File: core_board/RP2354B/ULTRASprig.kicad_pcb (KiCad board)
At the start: 2 copper layers, 34.1 x 53.9 mm, 47 parts, among them J1 Conn_01x06_Pin, J10 Conn_01x10_Pin, J2 USB_C_Receptacle_USB2.0_14P, J3 Conn_01x02_Pin, J4 Conn_01x12_Pin, J6 Conn_01x10_Pin, U1 RP2354B, U2 USBLC6-2P6, U3 BQ24230RGT, U4 TPS62130A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

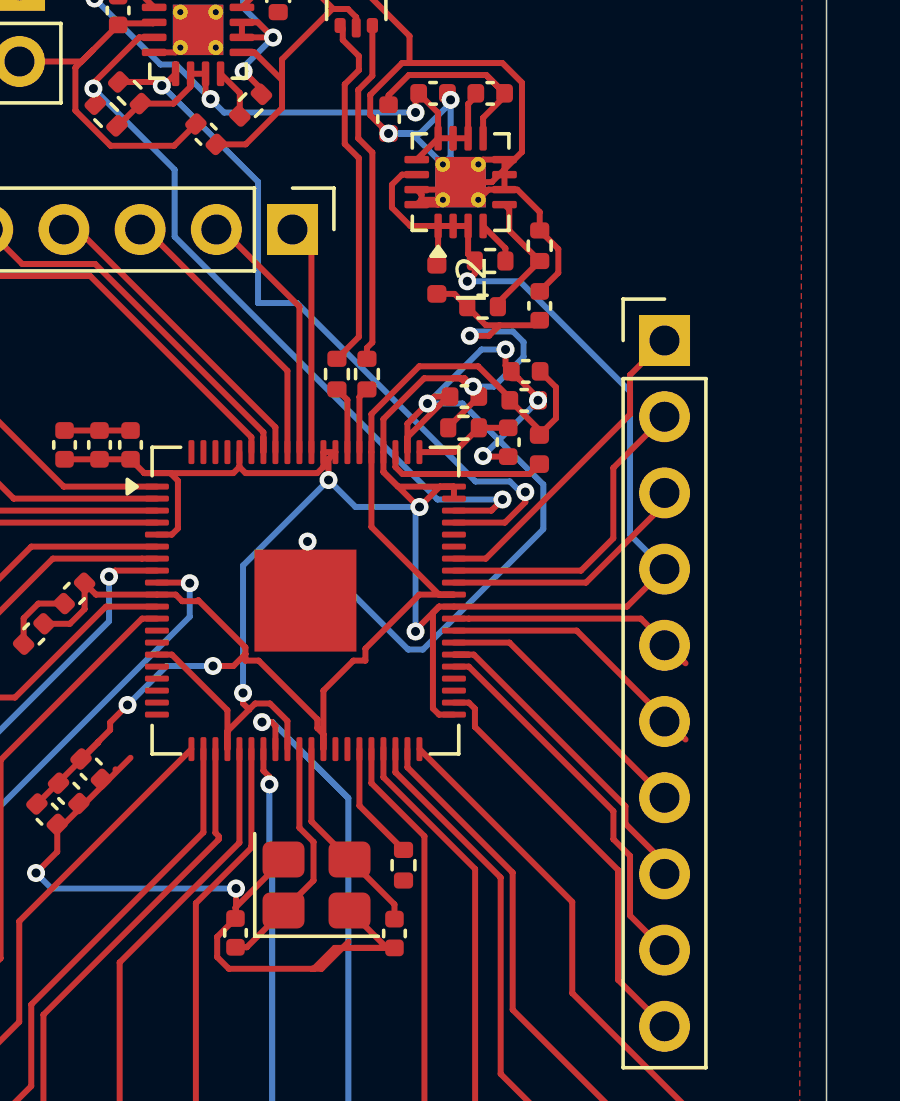
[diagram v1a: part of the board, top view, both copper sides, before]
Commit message: add RP2354 BoM
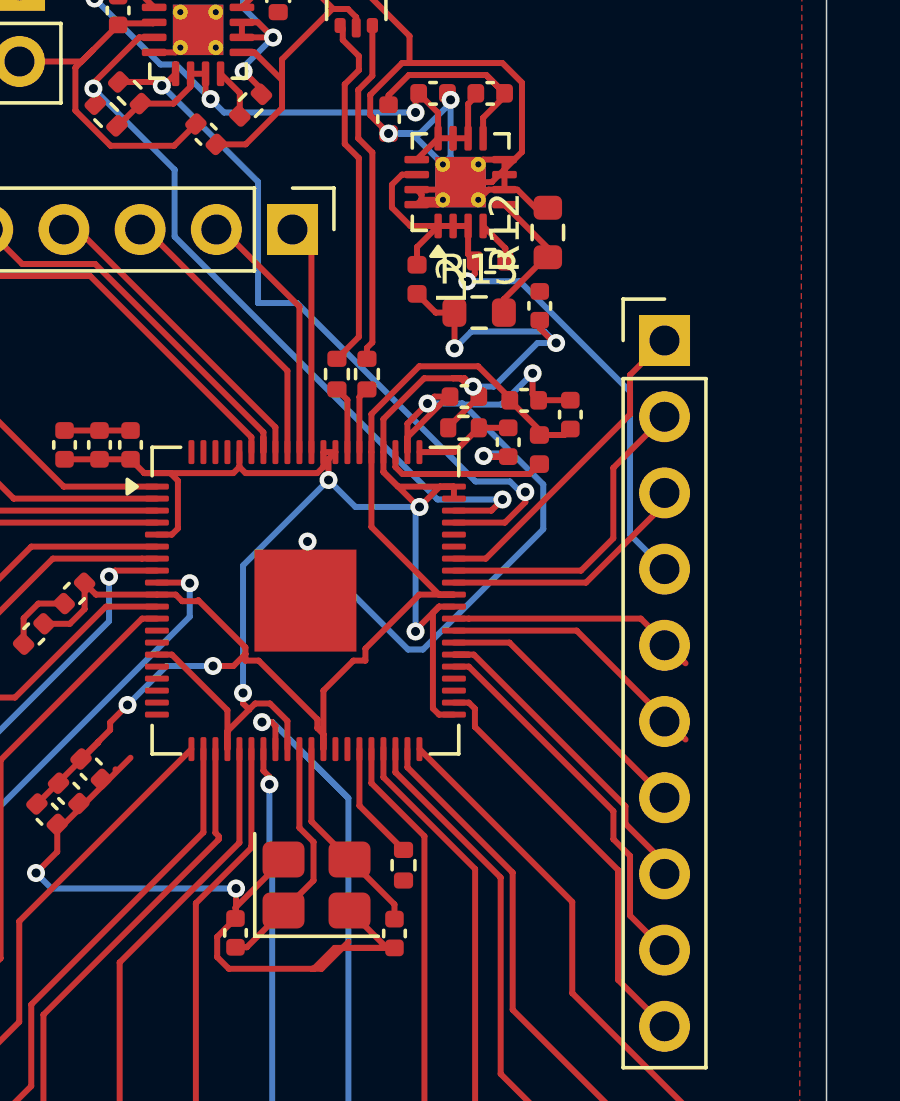
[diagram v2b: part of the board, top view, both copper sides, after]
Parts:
- R12: value 9K -> 8K; footprint Resistor_SMD:R_0402_1005Metric -> Resistor_SMD:R_0603_1608Metric
- R13: value 2K -> 25K; footprint Resistor_SMD:R_0402_1005Metric -> Resistor_SMD:R_0603_1608Metric
- moved C10 2.07 mm to (261.9, 133.5), turned to 90 degrees
- moved L2 0.66 mm to (256.8, 129.0)
- moved R12 0.52 mm to (261.1, 127.4)
- moved R13 0.23 mm to (258.8, 130.1)
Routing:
- net +3V3: track 77.1 -> 71.0 mm, vias 6 -> 7
- net GND: track 174.9 -> 170.4 mm, vias 14 -> 13
- net +1V1: track 48.4 -> 46.9 mm
- net Net-(U4-FB): track 4.34 -> 5.07 mm
